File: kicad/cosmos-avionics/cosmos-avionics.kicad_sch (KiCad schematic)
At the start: 20 parts, among them J1 Teensy D2-D5 (Vane Servo Out), J2 Teensy D18,19,23,1,9 (RC In, 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, J3 Teensy D10-13,20-22 (IMU SPI), J4 Teensy D8 (DShot to ESC), J5 Teensy Power (3V3,VIN,GND), J6 BNO085 IMU (CS,SCK,MOSI,MISO,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, J7 RC RX FS-iA6B (CH1-5,+5V,GND), M1 64mm EDF Motor (3-phase), SW1 Physical kill switch (>=80A), U1 Level Shifter #1 (RC CH1,CH2), U2 Level Shifter #2 (RC CH3,CH4,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, U3 UBEC 5V/5A (IN,OUT,GND)

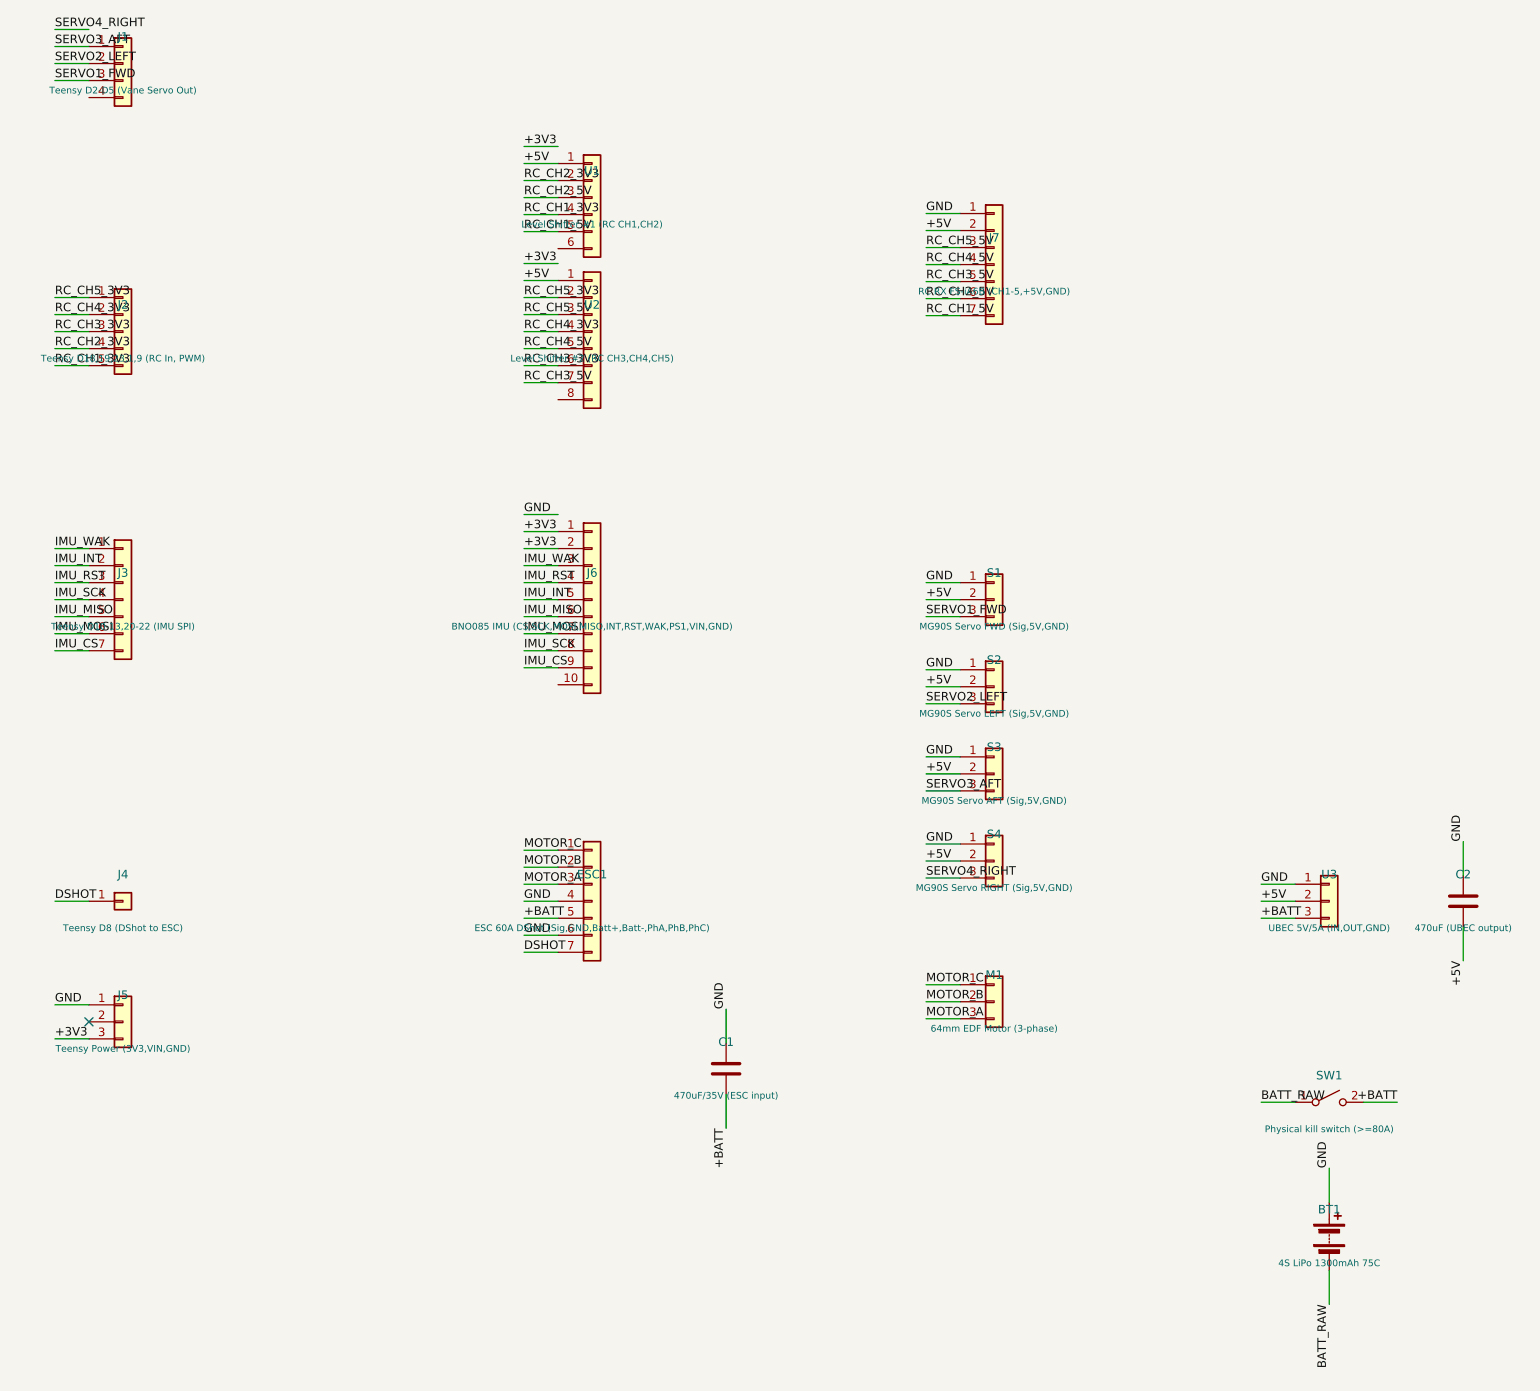
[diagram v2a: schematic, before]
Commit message: [kicad] 핀 좌표와 배선 방향을 고치고 실제 넷리스트를 검사
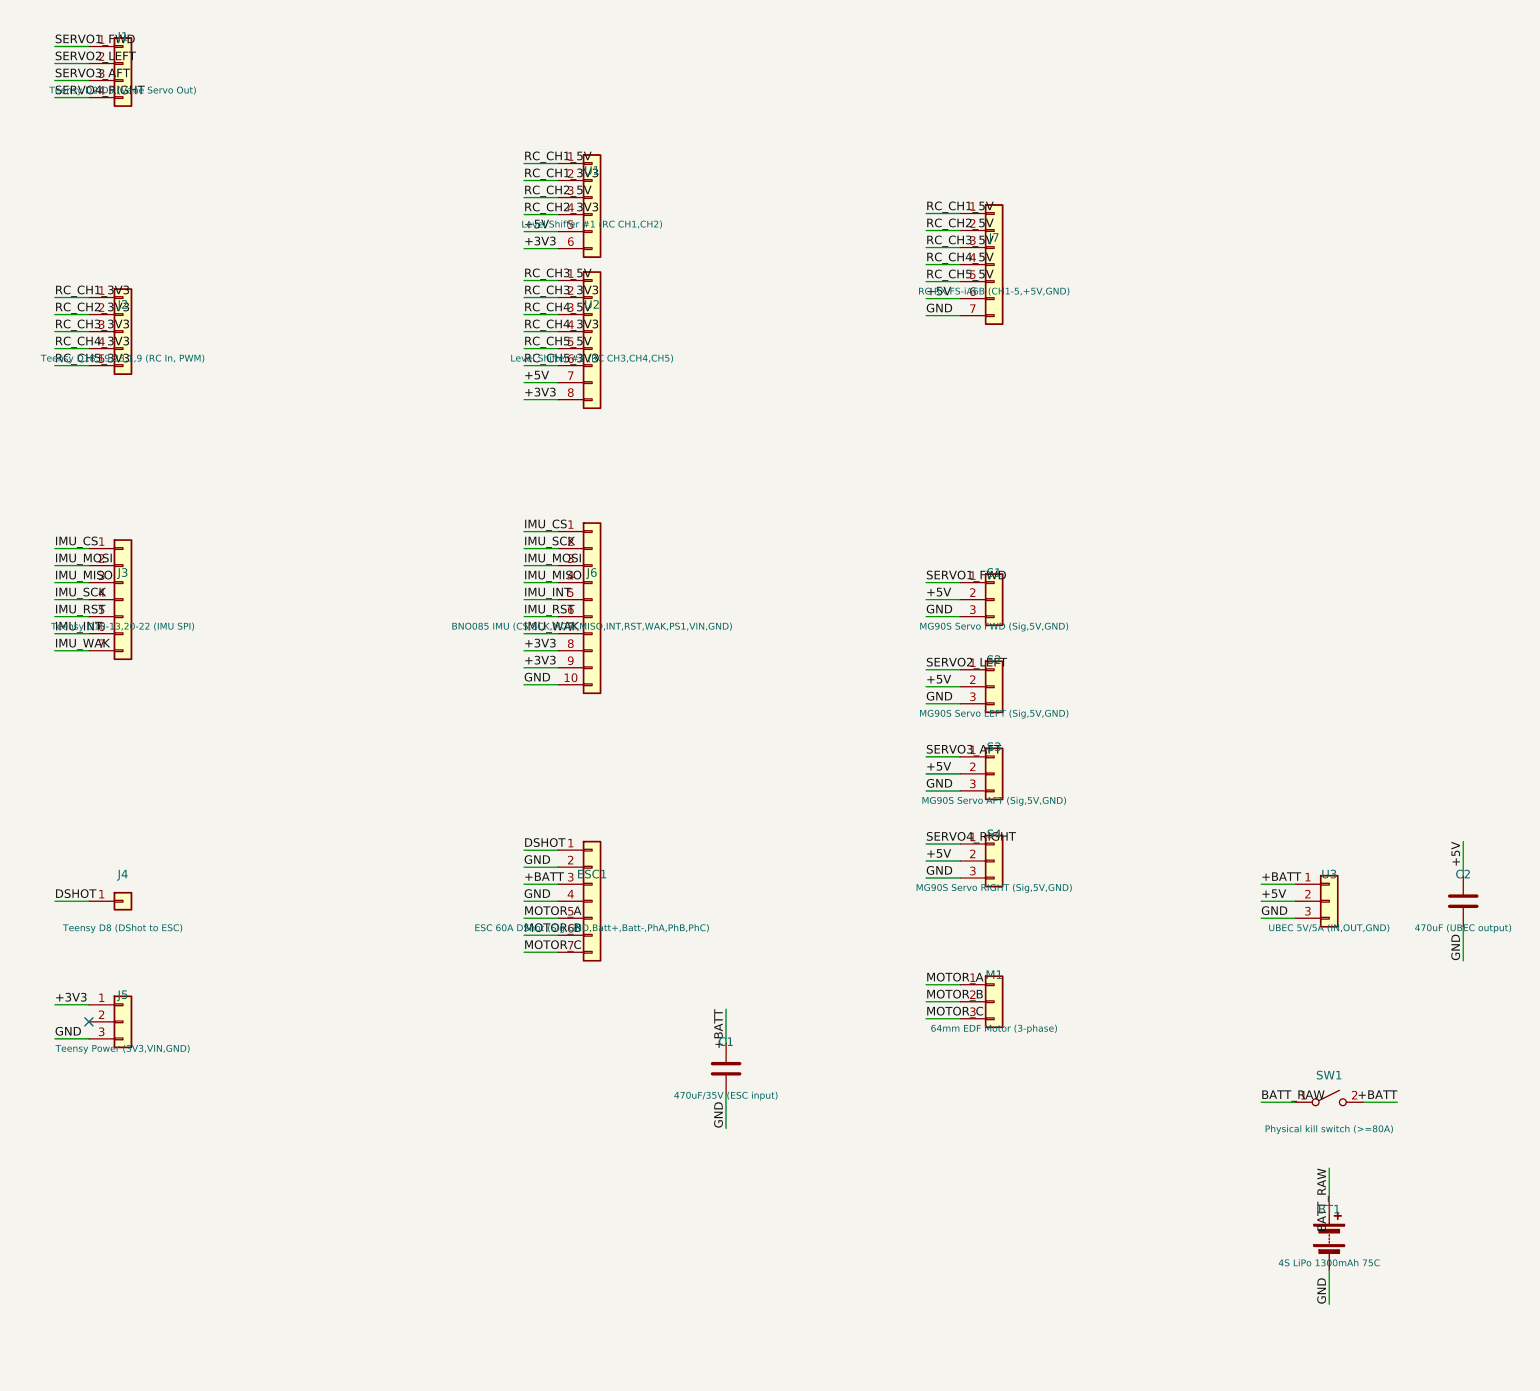
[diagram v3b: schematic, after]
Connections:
- net +3V3: now also J5.1 (Pin_1), J6.8 (Pin_8), J6.9 (Pin_9), U1.6 (Pin_6), U2.8 (Pin_8); no longer J5.3 (Pin_3), J6.1 (Pin_1), J6.2 (Pin_2)
- net +5V: now also C2.1, J7.6 (Pin_6), U1.5 (Pin_5), U2.7 (Pin_7); no longer C2.2, J7.2 (Pin_2), U1.1 (Pin_1), U2.1 (Pin_1)
- net +BATT: now also C1.1, ESC1.3 (Pin_3), U3.1 (Pin_1); no longer C1.2, ESC1.5 (Pin_5), U3.3 (Pin_3)
- net BATT_RAW: now also BT1.1 (+); no longer BT1.2 (-)
- net DSHOT: now also ESC1.1 (Pin_1); no longer ESC1.7 (Pin_7)
- net GND: now also BT1.2 (-), C1.2, C2.2, ESC1.2 (Pin_2), J5.3 (Pin_3), J6.10 (Pin_10), J7.7 (Pin_7), S1.3 (Pin_3), S2.3 (Pin_3), S3.3 (Pin_3), S4.3 (Pin_3), U3.3 (Pin_3); no longer BT1.1 (+), C1.1, C2.1, ESC1.6 (Pin_6), J5.1 (Pin_1), J7.1 (Pin_1), S1.1 (Pin_1), S2.1 (Pin_1), S3.1 (Pin_1), S4.1 (Pin_1), U3.1 (Pin_1)
- net IMU_CS: now also J3.1 (Pin_1), J6.1 (Pin_1); no longer J3.7 (Pin_7), J6.9 (Pin_9)
- net IMU_INT: now also J3.6 (Pin_6); no longer J3.2 (Pin_2)
- net IMU_MISO: now also J3.3 (Pin_3), J6.4 (Pin_4); no longer J3.5 (Pin_5), J6.6 (Pin_6)
- net IMU_MOSI: now also J3.2 (Pin_2), J6.3 (Pin_3); no longer J3.6 (Pin_6), J6.7 (Pin_7)
- net IMU_RST: now also J3.5 (Pin_5), J6.6 (Pin_6); no longer J3.3 (Pin_3), J6.4 (Pin_4)
- net IMU_SCK: now also J6.2 (Pin_2); no longer J6.8 (Pin_8)
- net IMU_WAK: now also J3.7 (Pin_7), J6.7 (Pin_7); no longer J3.1 (Pin_1), J6.3 (Pin_3)
- net MOTOR_A: now also ESC1.5 (Pin_5), M1.1 (Pin_1); no longer ESC1.3 (Pin_3), M1.3 (Pin_3)
- net MOTOR_B: now also ESC1.6 (Pin_6); no longer ESC1.2 (Pin_2)
- net MOTOR_C: now also ESC1.7 (Pin_7), M1.3 (Pin_3); no longer ESC1.1 (Pin_1), M1.1 (Pin_1)
- net RC_CH1_3V3: now also J2.1 (Pin_1), U1.2 (Pin_2); no longer J2.5 (Pin_5), U1.4 (Pin_4)
- net RC_CH1_5V: now also J7.1 (Pin_1), U1.1 (Pin_1); no longer J7.7 (Pin_7), U1.5 (Pin_5)
- net RC_CH2_3V3: now also J2.2 (Pin_2), U1.4 (Pin_4); no longer J2.4 (Pin_4), U1.2 (Pin_2)
- net RC_CH2_5V: now also J7.2 (Pin_2); no longer J7.6 (Pin_6)
- net RC_CH3_3V3: now also U2.2 (Pin_2); no longer U2.6 (Pin_6)
- net RC_CH3_5V: now also J7.3 (Pin_3), U2.1 (Pin_1); no longer J7.5 (Pin_5), U2.7 (Pin_7)
- net RC_CH4_3V3: now also J2.4 (Pin_4); no longer J2.2 (Pin_2)
- net RC_CH4_5V: now also U2.3 (Pin_3); no longer U2.5 (Pin_5)
- net RC_CH5_3V3: now also J2.5 (Pin_5), U2.6 (Pin_6); no longer J2.1 (Pin_1), U2.2 (Pin_2)
- net RC_CH5_5V: now also J7.5 (Pin_5), U2.5 (Pin_5); no longer J7.3 (Pin_3), U2.3 (Pin_3)
- net SERVO1_FWD: now also J1.1 (Pin_1), S1.1 (Pin_1); no longer J1.3 (Pin_3), S1.3 (Pin_3)
- net SERVO2_LEFT: now also S2.1 (Pin_1); no longer S2.3 (Pin_3)
- net SERVO3_AFT: now also J1.3 (Pin_3), S3.1 (Pin_1); no longer J1.1 (Pin_1), S3.3 (Pin_3)
- net SERVO4_RIGHT: now also J1.4 (Pin_4), S4.1 (Pin_1); no longer S4.3 (Pin_3)
